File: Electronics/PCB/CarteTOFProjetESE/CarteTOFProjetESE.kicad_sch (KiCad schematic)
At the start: 8 parts

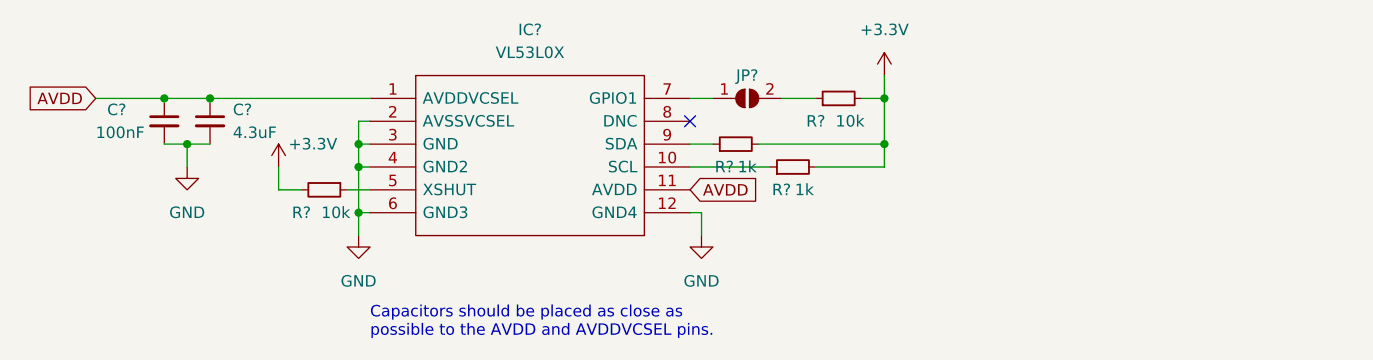
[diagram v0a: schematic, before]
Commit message: added test pin
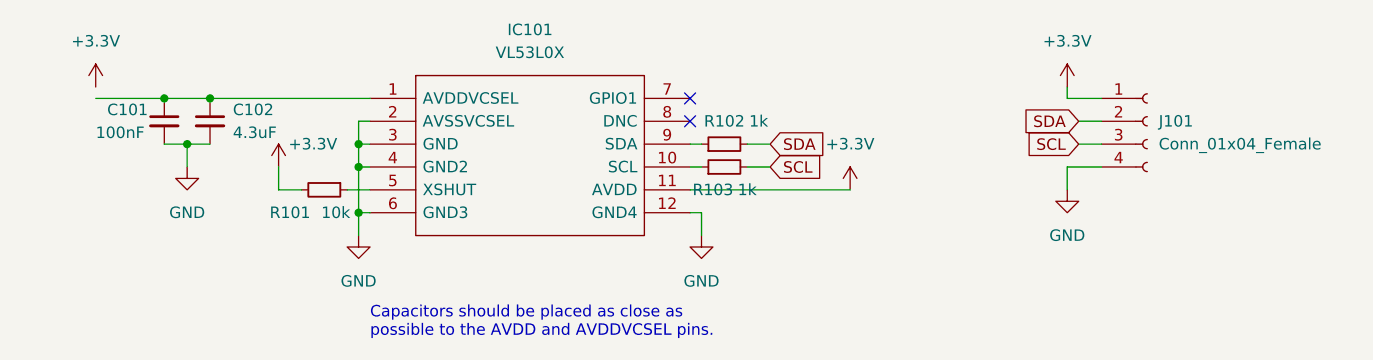
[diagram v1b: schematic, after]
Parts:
- removed JP?: (no value), symbol Jumper:SolderJumper_2_Open
- removed R?: 10k, symbol Device:R_Small
- added J101: Conn_01x04_Female, symbol Connector:Conn_01x04_Female
- gave numbers to parts that had none: 6
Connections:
- net +3.3V: now also IC101.11 (AVDD), J101.1 (Pin_1); no longer R102.2, R103.2
- net GND: now also J101.4 (Pin_4)
- net AVDD: no longer names the net of C101.1, C102.1, IC101.1 (AVDDVCSEL)
- net AVDD: no longer IC101.11 (AVDD)
- new net SCL: J101.3 (Pin_3), R103.2
- new net SDA: J101.2 (Pin_2), R102.2
- no-connect marks 1 -> 2
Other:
- moved on the sheet: R102, R103
